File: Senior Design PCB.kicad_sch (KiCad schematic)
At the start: 61 parts, among them J1 Conn_01x02, J2 Conn_01x02, J3 Raspberry_Pi_Zero_2W, J7-1 Conn_01x04, J7-2 Conn_01x04, U1 LM2678SX-5.0/NOPB, U2 MCP3008, U3 MAX38890

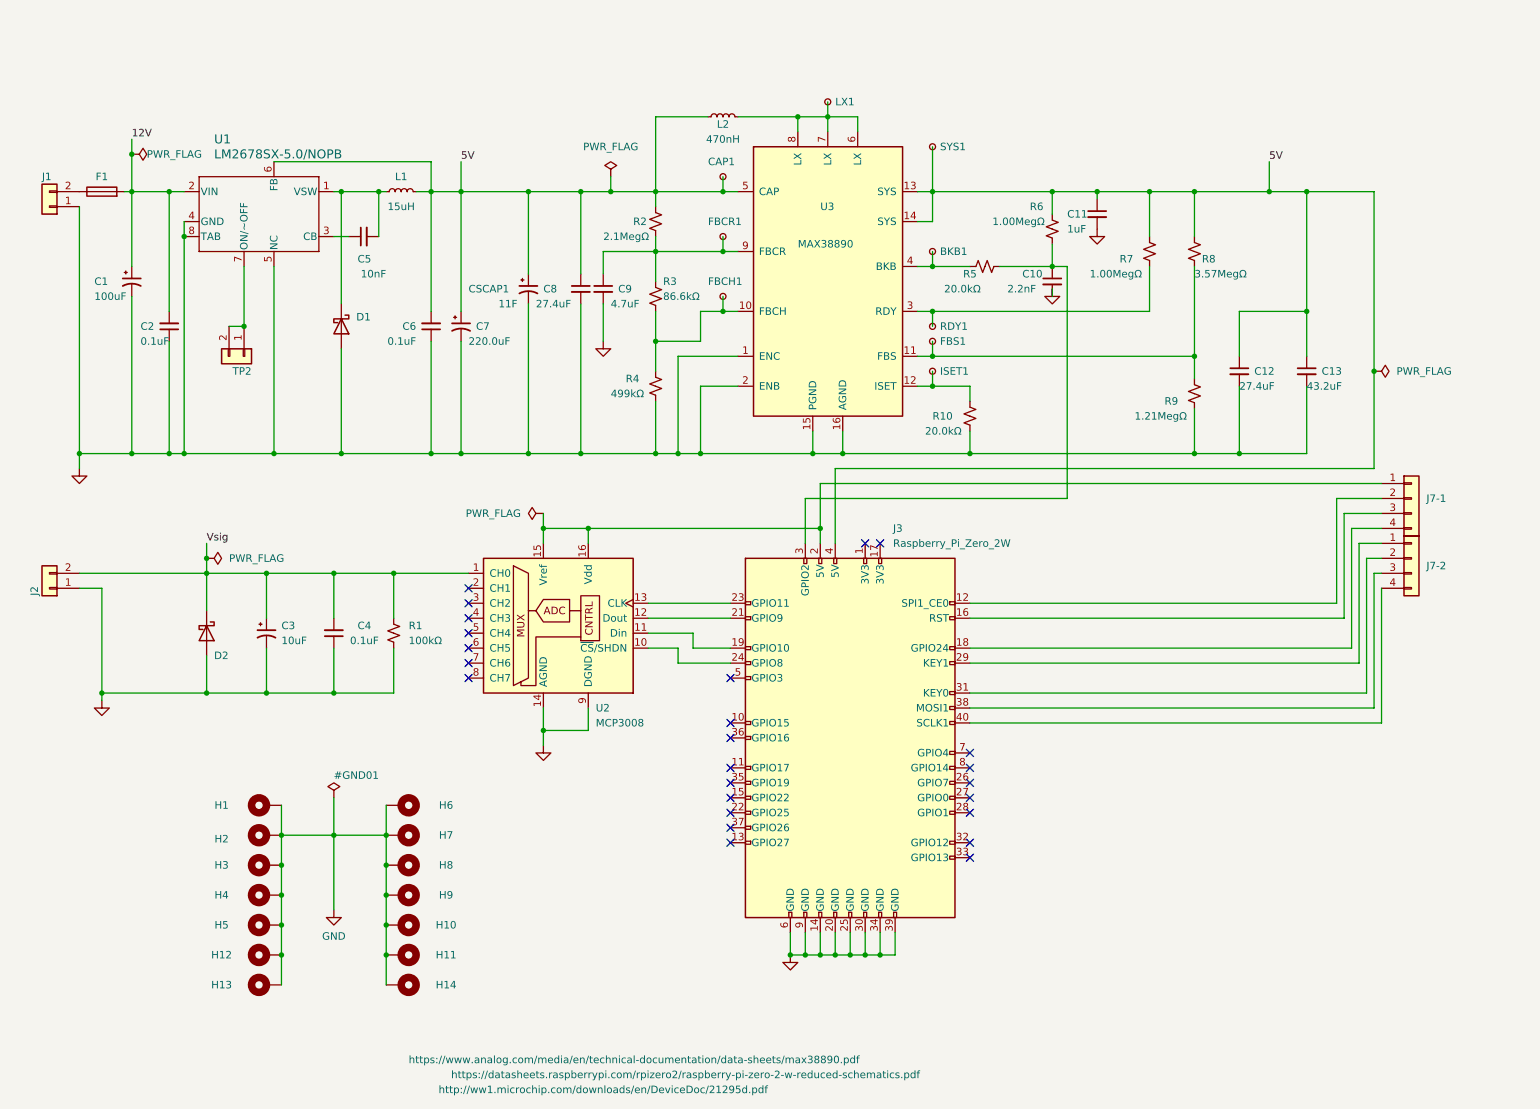
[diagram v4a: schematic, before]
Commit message: Mark Bruno edits implemented.
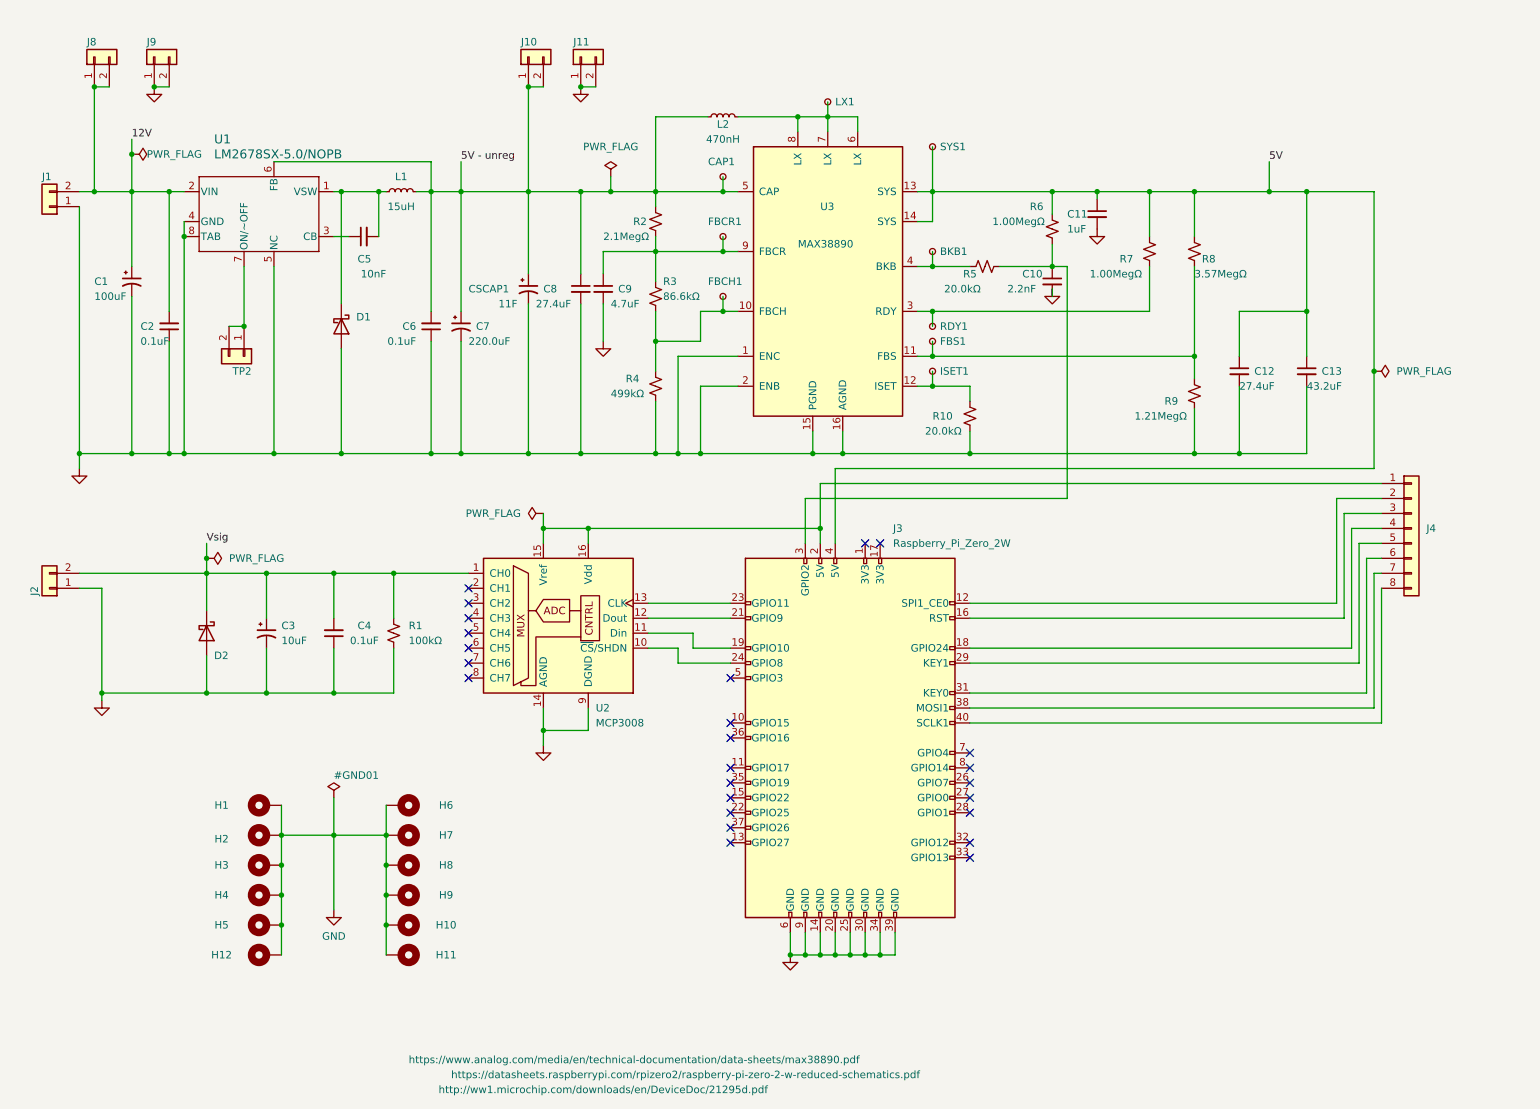
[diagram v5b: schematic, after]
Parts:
- removed F1: Fuse, AAA_senior_design:FUSE_4525, symbol Device:Fuse
- removed H13, H14: MountingHole_Pad, MountingHole:MountingHole_3.2mm_M3_Pad, symbol Mechanical:MountingHole_Pad
- removed J7-1, J7-2: Conn_01x04, Connector_PinSocket_2.54mm:PinSocket_1x04_P2.54mm_Vertical, symbol Connector_Generic:Conn_01x04
- added J10, J11, J8, J9: Conn_01x02, Connector_PinHeader_2.54mm:PinHeader_1x02_P2.54mm_Vertical, symbol Connector_Generic:Conn_01x02
- added J4: Conn_01x08, Connector_PinHeader_2.54mm:PinHeader_1x08_P2.54mm_Vertical, symbol Connector_Generic:Conn_01x08
- H1, H10, H11, H12, H2, H3, H4, H5, H6, H7, H8, H9: footprint MountingHole:MountingHole_3.2mm_M3_Pad -> MountingHole:MountingHole_3.2mm_M3_DIN965_Pad
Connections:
- net 12V: now also J1.2 (Pin_2), J8.1 (Pin_1), J8.2 (Pin_2)
- net 5V: no longer C6.2, C7.1, C8.1, CAP1.1, CSCAP1.1, L1.2, L2.1, R2.1, U1.6 (FB), U3.5 (CAP)
- net GND: now also J11.1 (Pin_1), J11.2 (Pin_2), J9.1 (Pin_1), J9.2 (Pin_2)
- net at J3.29 (KEY1): now also J4.5 (Pin_5)
- net at J3.31 (KEY0): now also J4.6 (Pin_6)
- net at J3.38 (MOSI1): now also J4.7 (Pin_7)
- net at J3.40 (SCLK1): now also J4.8 (Pin_8)
- net at J3.2 (5V), U2.15 (Vref), U2.16 (Vdd): now also J4.1 (Pin_1)
- net at J3.12 (SPI1_CE0): now also J4.2 (Pin_2)
- net at J3.16 (RST): now also J4.3 (Pin_3)
- net at J3.18 (GPIO24): now also J4.4 (Pin_4)
- new net 5V - unreg: C6.2, C7.1, C8.1, CAP1.1, CSCAP1.1, J10.1 (Pin_1), J10.2 (Pin_2), L1.2, L2.1, R2.1, U1.6 (FB), U3.5 (CAP)
